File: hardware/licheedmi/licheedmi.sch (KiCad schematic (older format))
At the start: 64 parts, among them J1 Conn_01x07, J2 HDMI_A_PCB, J3 LicheePiNano_LCD, J4 HDMI_A, U1 TDA19988, U2 LicheeNano, U3 TS3DV20812, U4 SC6206B

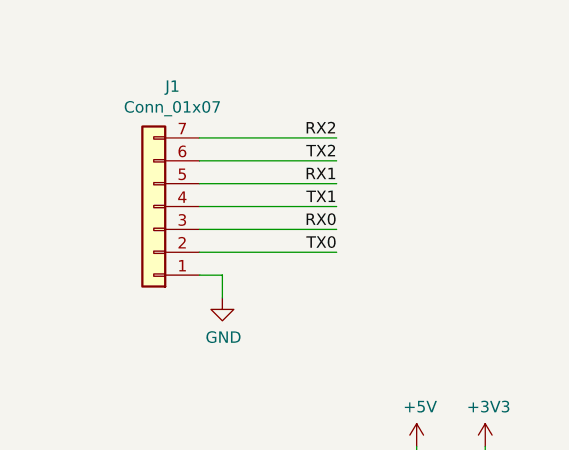
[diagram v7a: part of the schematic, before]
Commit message: sch, pcb: Add 3V3 and 5V headers
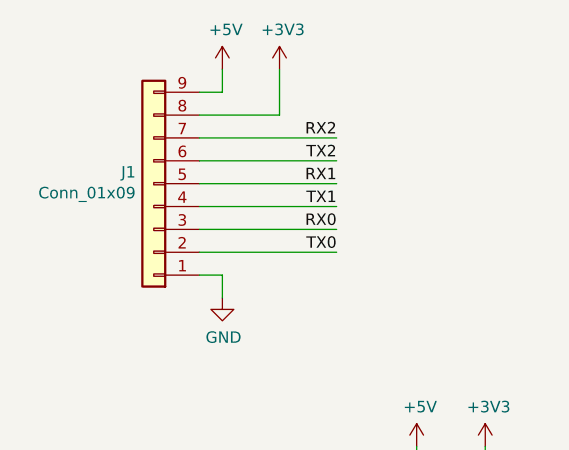
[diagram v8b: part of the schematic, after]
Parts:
- removed J1: Conn_01x07, Connector_PinHeader_2.54mm:PinHeader_1x07_P2.54mm_Vertical, symbol Connector_Generic:Conn_01x07
- added J1: Conn_01x09, Connector_PinHeader_2.54mm:PinHeader_1x09_P2.54mm_Vertical, symbol Connector_Generic:Conn_01x09
- U2: LCSC P/N (none) -> C35445; MFR P/N (none) -> C35445
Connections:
- net +3V3: now also J1.8 (Pin_8)
- net +5V: now also J1.9 (Pin_9)
- net GND: now also J1.1 (Pin_1)
- net RX0: now also J1.3 (Pin_3)
- net RX1: now also J1.5 (Pin_5)
- net RX2: now also J1.7 (Pin_7)
- net TX0: now also J1.2 (Pin_2)
- net TX1: now also J1.4 (Pin_4)
- net TX2: now also J1.6 (Pin_6)
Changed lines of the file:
@@
 F 2 "hdmizness:LicheeNano" H 1500 2650 50  0001 C CNN
 F 3 "${KIPRJMOD}/../../documentation/lichee_nano_8.16_schematic.pdf" H 1500 2650 50  0001 C CNN
+F 4 "C35445" H 1750 2600 50  0001 C CNN "LCSC P/N"
+F 5 "C35445" H 1750 2600 50  0001 C CNN "MFR P/N"
 	1    1750 2600
 	1    0    0    -1
@@
 	0    -1   -1   0
 $EndComp
-$Comp
-L Connector_Generic:Conn_01x07 J1
-U 1 1 613C8FAC
-P 1500 1350
-F 0 "J1" H 1418 825 50  0000 C CNN
-F 1 "Conn_01x07" H 1418 916 50  0000 C CNN
-F 2 "Connector_PinHeader_2.54mm:PinHeader_1x07_P2.54mm_Vertical" H 1500 1350 50  0001 C CNN
-F 3 "~" H 1500 1350 50  0001 C CNN
-F 4 "C225482" H 1500 1350 50  0001 C CNN "LCSC P/N"
-F 5 "A2541WV-7P" H 1500 1350 50  0001 C CNN "MFR P/N"
-	1    1500 1350
-	-1   0    0    1
-$EndComp
 Wire Wire Line
 	1700 1650 1800 1650
@@
 Wire Wire Line
 	4300 10100 4400 10100
+$Comp
+L Connector_Generic:Conn_01x09 J1
+U 1 1 5EDD1EBB
+P 1500 1250
+F 0 "J1" H 1579 1200 50  0000 L CNN
+F 1 "Conn_01x09" H 1579 1291 50  0000 L CNN
+F 2 "Connector_PinHeader_2.54mm:PinHeader_1x09_P2.54mm_Vertical" H 1500 1250 50  0001 C CNN
+F 3 "~" H 1500 1250 50  0001 C CNN
+F 4 "C225484" H 1500 1250 50  0001 C CNN "LCSC P/N"
+F 5 "A2541WV-9P" H 1500 1250 50  0001 C CNN "MFR P/N"
+	1    1500 1250
+	-1   0    0    1
+$EndComp
+$Comp
+L power:+5V #PWR037
+U 1 1 5EDD6193
+P 1800 750
+F 0 "#PWR037" H 1800 600 50  0001 C CNN
+F 1 "+5V" H 1815 923 50  0000 C CNN
+F 2 "" H 1800 750 50  0001 C CNN
+F 3 "" H 1800 750 50  0001 C CNN
+	1    1800 750
+	1    0    0    -1
+$EndComp
+$Comp
+L power:+3V3 #PWR038
+U 1 1 5EDD6B30
+P 2050 750
+F 0 "#PWR038" H 2050 600 50  0001 C CNN
+F 1 "+3V3" H 2065 923 50  0000 C CNN
+F 2 "" H 2050 750 50  0001 C CNN
+F 3 "" H 2050 750 50  0001 C CNN
+	1    2050 750
+	1    0    0    -1
+$EndComp
+Wire Wire Line
+	1700 850  1800 850
+Wire Wire Line
+	1800 850  1800 750
+Wire Wire Line
+	1700 950  2050 950
+Wire Wire Line
+	2050 950  2050 750
 $EndSCHEMATC
